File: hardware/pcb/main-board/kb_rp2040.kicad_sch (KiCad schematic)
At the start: 27 parts, among them J1201 Conn_01x02, U1202 W25Q128JVS, U1203 RP2040, Y1201 ABLS-12.000MHZ-B4-T

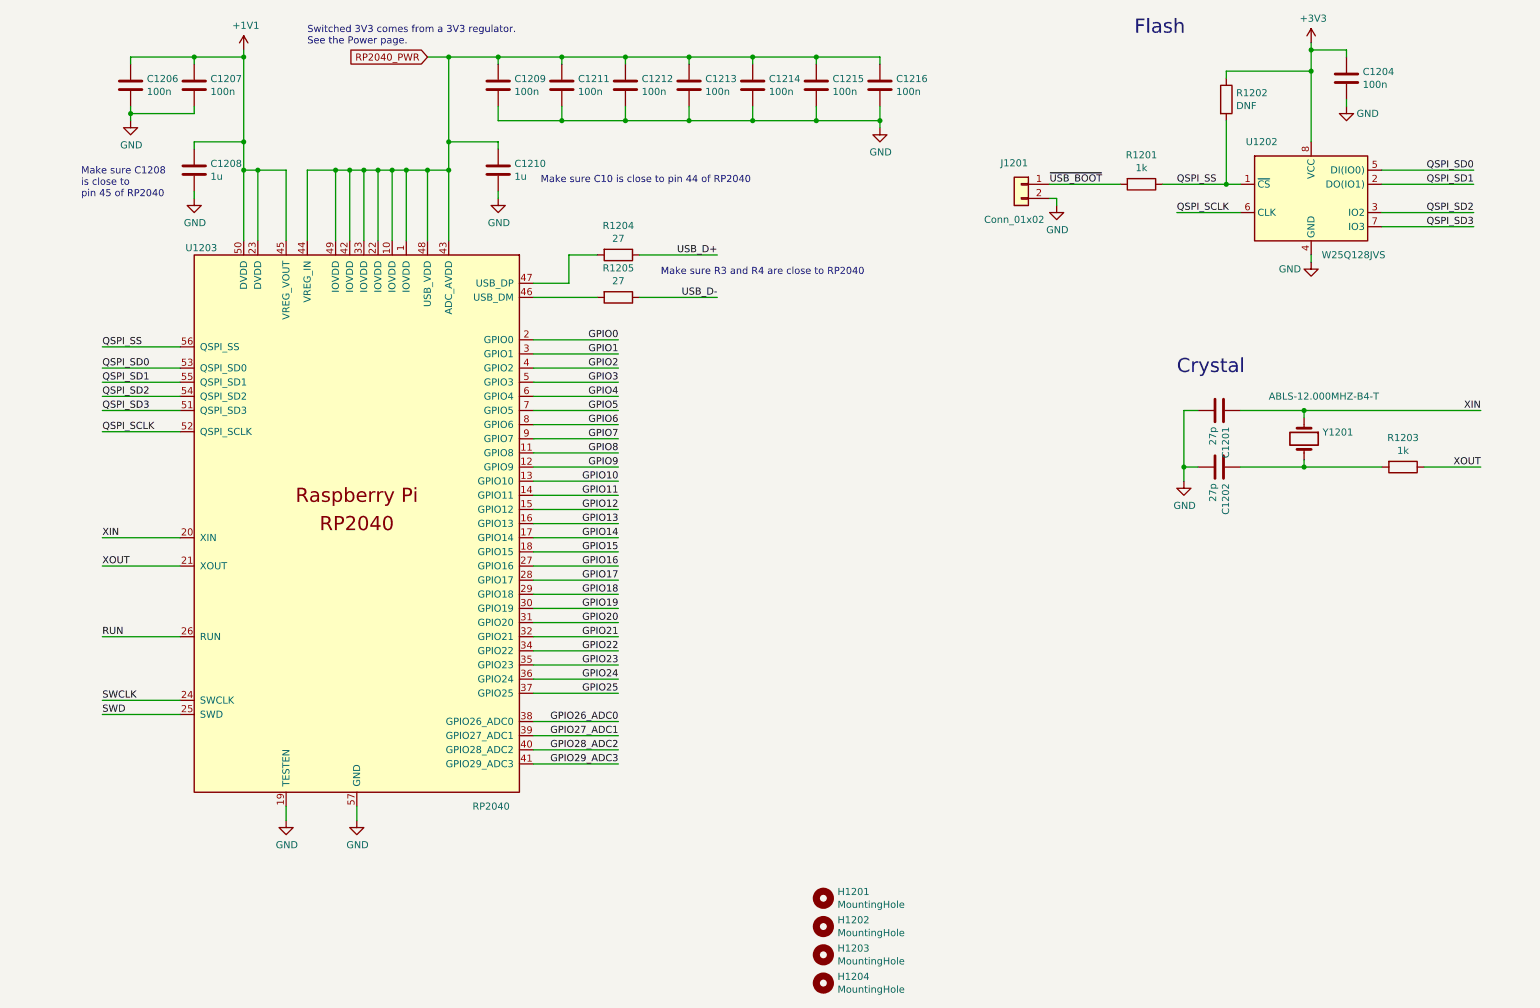
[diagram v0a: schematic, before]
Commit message: more work on KB pico replacement
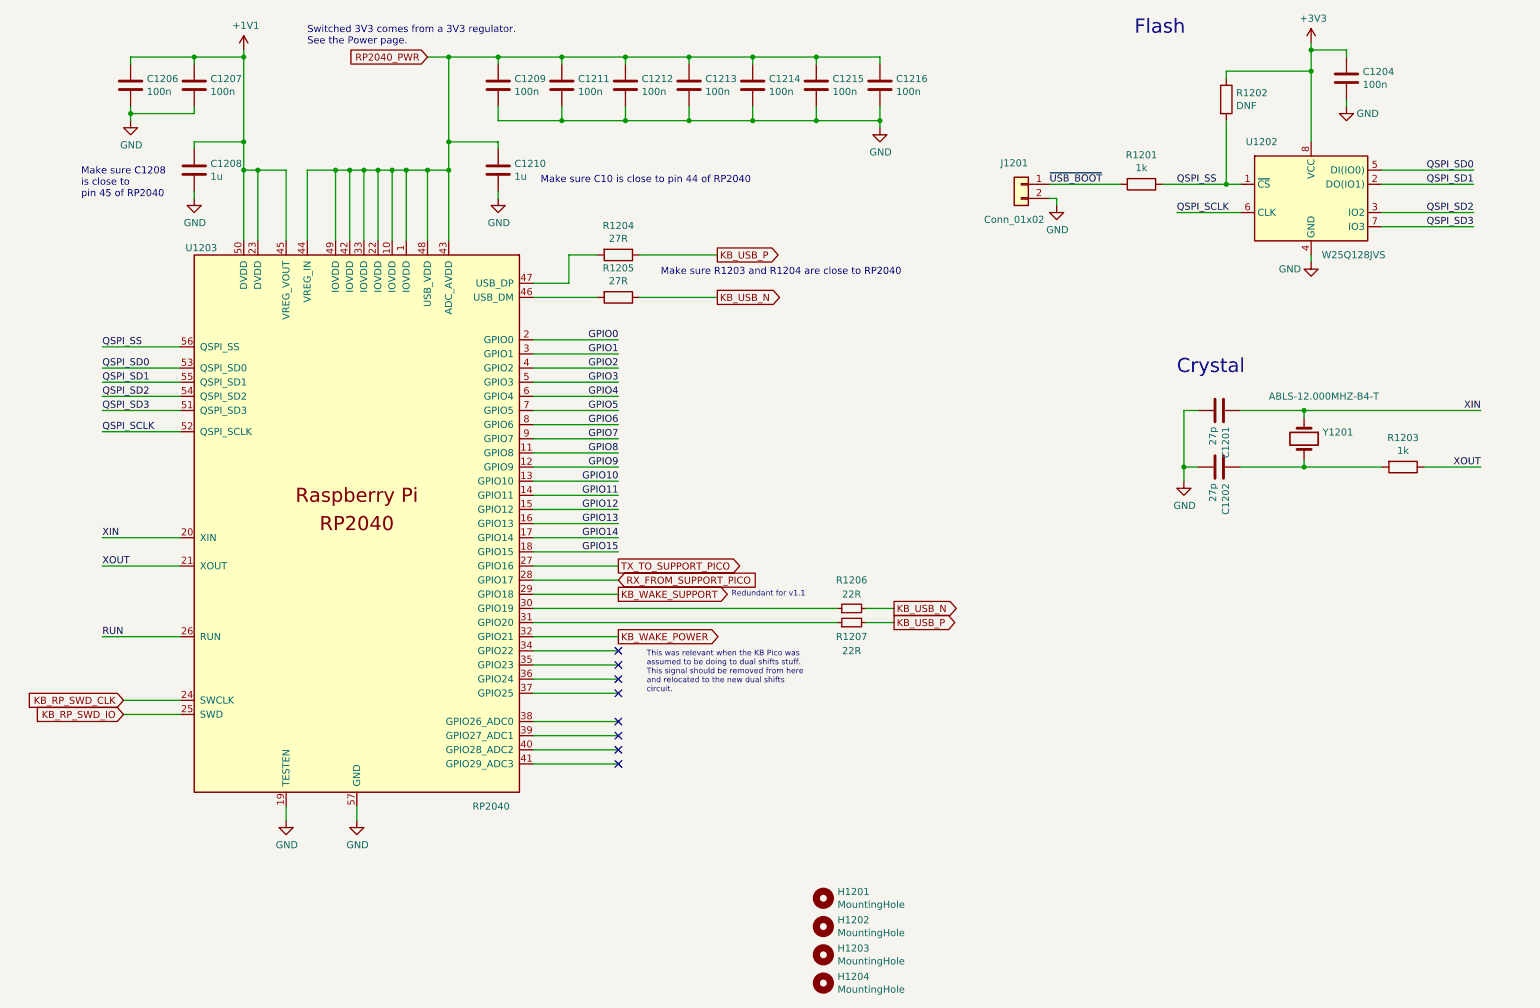
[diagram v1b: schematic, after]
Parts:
- added R1206, R1207: 22R, Resistor_SMD:R_0805_2012Metric_Pad1.20x1.40mm_HandSolder, symbol Device:R_Small
- R1204, R1205: value 27 -> 27R
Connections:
- net GPIO16 renamed TX_TO_SUPPORT_PICO
- net GPIO17 renamed RX_FROM_SUPPORT_PICO
- net GPIO18 renamed KB_WAKE_SUPPORT
- net GPIO19: no longer names the net of U1203.30 (GPIO19)
- net GPIO19: now also R1206.1
- net GPIO20: no longer names the net of U1203.31 (GPIO20)
- net GPIO20: now also R1207.1
- net GPIO21 renamed KB_WAKE_POWER
- net GPIO22: no longer names the net of U1203.34 (GPIO22)
- net GPIO23: no longer names the net of U1203.35 (GPIO23)
- net GPIO24: no longer names the net of U1203.36 (GPIO24)
- net GPIO25: no longer names the net of U1203.37 (GPIO25)
- net GPIO26_ADC0: no longer names the net of U1203.38 (GPIO26_ADC0)
- net GPIO27_ADC1: no longer names the net of U1203.39 (GPIO27_ADC1)
- net GPIO28_ADC2: no longer names the net of U1203.40 (GPIO28_ADC2)
- net GPIO29_ADC3: no longer names the net of U1203.41 (GPIO29_ADC3)
- net SWCLK renamed KB_RP_SWD_CLK
- net SWD renamed KB_RP_SWD_IO
- net USB_D+ renamed KB_USB_P
- net KB_USB_P: now also R1207.2
- net USB_D- renamed KB_USB_N
- net KB_USB_N: now also R1206.2
- no-connect marks 0 -> 8
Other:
- note added: "Make sure R1203 and R1204 are close to RP2040"
- note added: "Redundant for v1.1"
- note added: "This was relevant when the KB Pico was assumed to be doing to dual shifts stuff. This signal should be removed from here and relocated to the new dual shifts circuit."
- note removed: "Make sure R3 and R4 are close to RP2040"

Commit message: more working out of the KB pico replacement
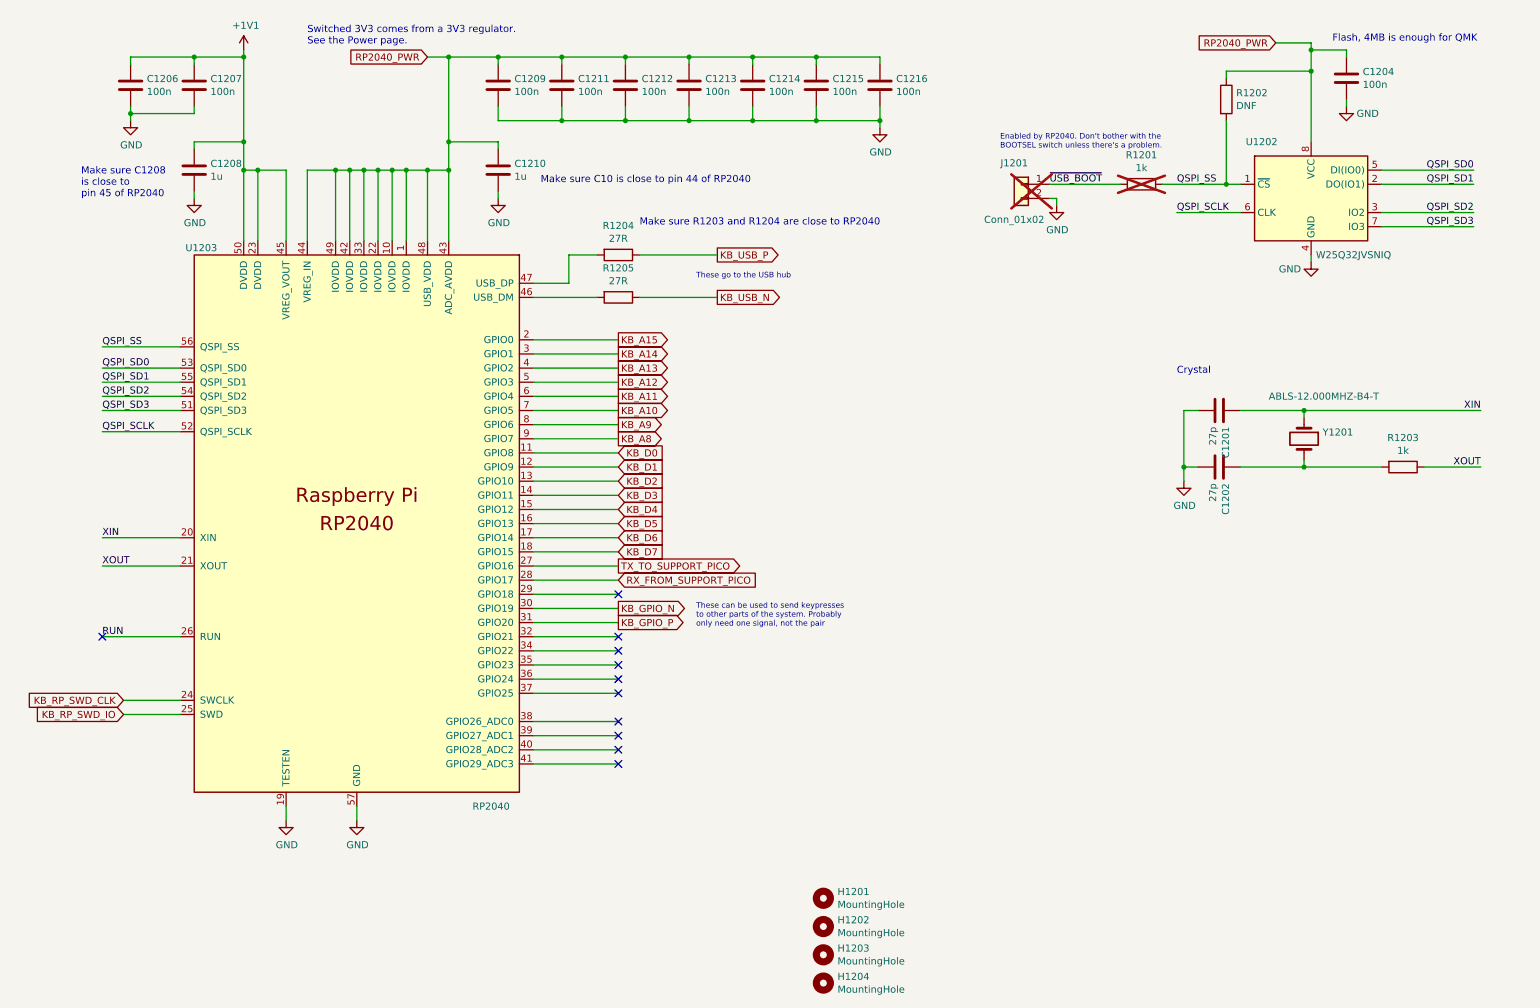
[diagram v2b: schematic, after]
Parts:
- removed R1206, R1207: 22R, Resistor_SMD:R_0805_2012Metric_Pad1.20x1.40mm_HandSolder, symbol Device:R_Small
- J1201, R1201: now not fitted
- U1202: value W25Q128JVS -> W25Q32JVSNIQ
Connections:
- net +3V3 is gone; now on net RP2040_PWR: C1204.1, R1202.1, U1202.8 (VCC)
- net KB_GPIO_N: now reaches U1203.30 (GPIO19)
- net KB_GPIO_P: now reaches U1203.31 (GPIO20)
- net GPIO0 renamed KB_A15
- net GPIO1 renamed KB_A14
- net GPIO10 renamed KB_D2
- net GPIO11 renamed KB_D3
- net GPIO12 renamed KB_D4
- net GPIO13 renamed KB_D5
- net GPIO14 renamed KB_D6
- net GPIO15 renamed KB_D7
- net GPIO2 renamed KB_A13
- net GPIO3 renamed KB_A12
- net GPIO4 renamed KB_A11
- net GPIO5 renamed KB_A10
- net GPIO6 renamed KB_A9
- net GPIO7 renamed KB_A8
- net GPIO8 renamed KB_D0
- net GPIO9 renamed KB_D1
- net KB_WAKE_POWER: no longer names the net of U1203.32 (GPIO21)
- net KB_WAKE_SUPPORT: no longer names the net of U1203.29 (GPIO18)
- no-connect marks 8 -> 11
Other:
- note added: "Enabled by RP2040. Don't bother with the BOOTSEL switch unless there's a problem."
- note added: "Flash, 4MB is enough for QMK"
- note added: "These can be used to send keypresses to other parts of the system. Probably only need one signal, not the pair"
- note added: "These go to the USB hub"
- note removed: "Flash"
- note removed: "Redundant for v1.1"
- note removed: "This was relevant when the KB Pico was assumed to be doing to dual shifts stuff. This signal should be removed from here and relocated to the new dual shifts circuit."

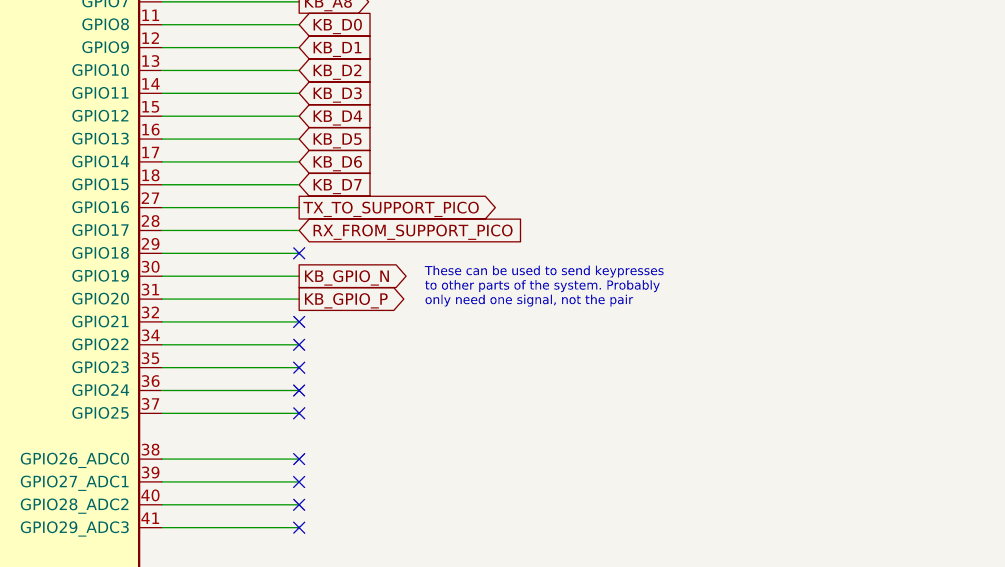
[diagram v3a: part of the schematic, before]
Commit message: rename the pico bits to RP2040, still a few things to check
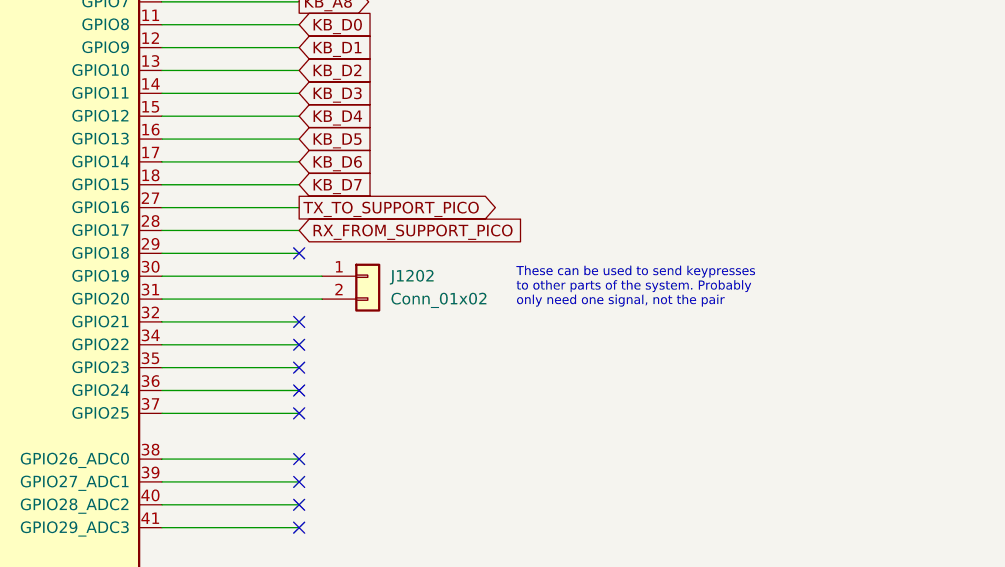
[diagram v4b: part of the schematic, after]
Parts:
- added J1202: Conn_01x02, symbol Connector_Generic:Conn_01x02
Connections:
- net KB_GPIO_N: no longer names the net of U1203.30 (GPIO19)
- net KB_GPIO_N: now also J1202.1 (Pin_1)
- net KB_GPIO_P: no longer names the net of U1203.31 (GPIO20)
- net KB_GPIO_P: now also J1202.2 (Pin_2)
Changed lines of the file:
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@@
 	(wire
 		(pts
-			(xy 105.41 125.73) (xy 120.65 125.73)
+			(xy 105.41 125.73) (xy 123.19 125.73)
 		)
 		(stroke
@@
 	(wire
 		(pts
-			(xy 105.41 128.27) (xy 120.65 128.27)
+			(xy 105.41 128.27) (xy 123.19 128.27)
 		)
 		(stroke
@@
 	(text "These can be used to send keypresses\nto other parts of the system. Probably\nonly need one signal, not the pair"
 		(exclude_from_sim no)
-		(at 134.62 127 0)
+		(at 144.78 127 0)
 		(effects
 			(font
@@
 		)
 	)
-	(global_label "KB_GPIO_N"
-		(shape output)
-		(at 120.65 125.73 0)
-		(fields_autoplaced yes)
-		(effects
-			(font
-				(size 1.27 1.27)
-			)
-			(justify left)
-		)
-		(property "Intersheetrefs" "${INTERSHEET_REFS}"
-			(at 133.262 125.73 0)
-			(effects
-				(font
-					(size 1.27 1.27)
-				)
-				(justify left)
-				(hide yes)
-			)
-		)
-	)
 	(global_label "KB_D0"
 		(shape input)
@@
 		)
 	)
-	(global_label "KB_GPIO_P"
-		(shape output)
-		(at 120.65 128.27 0)
-		(fields_autoplaced yes)
-		(effects
-			(font
-				(size 1.27 1.27)
-			)
-			(justify left)
-		)
-		(property "Intersheetrefs" "${INTERSHEET_REFS}"
-			(at 133.2015 128.27 0)
-			(effects
-				(font
-					(size 1.27 1.27)
-				)
-				(justify left)
-				(hide yes)
-			)
-		)
-	)
 	(global_label "KB_A13"
 		(shape output)
@@
 					(unit 1)
 				)
+			)
+		)
+	)
+	(symbol
+		(lib_id "Connector_Generic:Conn_01x02")
+		(at 128.27 125.73 0)
+		(unit 1)
+		(exclude_from_sim no)
+		(in_bom yes)
+		(on_board yes)
+		(dnp no)
+		(fields_autoplaced yes)
+		(property "Reference" "J1202"
+			(at 130.81 125.7299 0)
+			(effects
+				(font
+					(size 1.27 1.27)
+				)
+				(justify left)
+			)
+		)
+		(property "Value" "Conn_01x02"
+			(at 130.81 128.2699 0)
+			(effects
+				(font
+					(size 1.27 1.27)
+				)
+				(justify left)
+			)
+		)
+		(property "Footprint" ""
+			(at 128.27 125.73 0)
+			(effects
+				(font
+					(size 1.27 1.27)
+				)
+				(hide yes)
+			)
+		)
+		(property "Datasheet" "~"
+			(at 128.27 125.73 0)
+			(effects
+				(font
+					(size 1.27 1.27)
+				)
+				(hide yes)
+			)
+		)
+		(property "Description" "Generic connector, single row, 01x02, script generated (kicad-library-utils/schlib/autogen/connector/)"
+			(at 128.27 125.73 0)
+			(effects
+				(font
+					(size 1.27 1.27)
+				)
+				(hide yes)
+			)
+		)
+		(pin "2"
+		)
+		(pin "1"
+		)
+		(instances
+			(project ""
+				(path "/fdce8012-5f35-4f58-8abb-80214b4af8fe/bd010eea-67e1-4f0f-9c21-5375d46a1c97"
+					(reference "J1202")
+					(unit 1)
+				)

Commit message: a few more tidyups, almost ready for dual shifts stuff now
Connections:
- net RP2040_PWR renamed RP2040_3V3_PWR
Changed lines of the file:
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@@
 		)
 	)
-	(global_label "RP2040_PWR"
+	(global_label "RP2040_3V3_PWR"
 		(shape input)
 		(at 86.36 26.67 180)
@@
 		)
 	)
-	(global_label "RP2040_PWR"
+	(global_label "RP2040_3V3_PWR"
 		(shape input)
 		(at 238.76 24.13 180)

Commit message: more support rp2040 cleanups
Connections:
- net RX_FROM_SUPPORT_PICO renamed RX_FROM_SP_RP
- net TX_TO_SUPPORT_PICO renamed TX_TO_SP_RP
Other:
- note added: "UART connection to the support RP2040. That device will need to receive keypresses and forward them to the application board."
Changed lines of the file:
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@@
+		)
+	)
+	(text "UART connection to the support RP2040.\nThat device will need to receive\nkeypresses and forward them to the\napplication board."
+		(exclude_from_sim no)
+		(at 144.78 119.38 0)
+		(effects
+			(font
+				(size 1 1)
+			)
+			(justify left)
 		)
 	)
@@
 		)
 	)
-	(global_label "TX_TO_SUPPORT_PICO"
+	(global_label "TX_TO_SP_RP"
 		(shape output)
 		(at 120.65 118.11 0)
@@
 		)
 		(property "Intersheetrefs" "${INTERSHEET_REFS}"
-			(at 143.4824 118.11 0)
+			(at 135.3785 118.11 0)
 			(effects
 				(font
@@
 		)
 	)
-	(global_label "RX_FROM_SUPPORT_PICO"
+	(global_label "RX_FROM_SP_RP"
 		(shape input)
 		(at 120.65 120.65 0)
@@
 		)
 		(property "Intersheetrefs" "${INTERSHEET_REFS}"
-			(at 146.6272 120.65 0)
-			(effects
-				(font
+			(at 138.5233 120.65 0)
+			(effects
+				(font
